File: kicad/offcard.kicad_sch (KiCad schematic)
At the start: 25 parts, among them IC1 NAU7802KGI, J10 lower fan, J4 heater, J5 5kg load cell, J6 LCD, J7 upper fan, Q2 SSM3K127TU, Q3 T1210-800G

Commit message: v1.7.0 upgrade most C/R to 1206 from 0805
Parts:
- R1, R12, R5: footprint PCM_Resistor_SMD_AKL:R_0805_2012Metric_Pad1.15x1.40mm_HandSolder -> Resistor_SMD:R_1206_3216Metric_Pad1.30x1.75mm_HandSolder
- R2, R3, R4: footprint Resistor_SMD:R_0805_2012Metric_Pad1.20x1.40mm_HandSolder -> Resistor_SMD:R_1206_3216Metric_Pad1.30x1.75mm_HandSolder
- R7: footprint PCM_Resistor_SMD_AKL:R_0805_2012Metric_Pad1.15x1.40mm_HandSolder -> PCM_Resistor_SMD_AKL:R_1206_3216Metric_Pad1.30x1.75mm_HandSolder
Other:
- note added: "2A/4A max continuous/pulse drain current. 10mA max current to MOSFET: 3.3V / 0.01A = 330Ω (0.033W). Schottky diode across motor +/- for EMP protection. Greartisan draws 0.18A at 12V (2.16W) in steady state. Can possibly eliminate R7 if MotorPin is always OUTPUT."
- note removed: "2A/4A max continuous/pulse drain current. 10mA max current to MOSFET: 3.3V / 0.01A = 330Ω (0.033W). Schottky diode across motor +/- for EMP protection. Greartisan draws 0.18A at 12V (2.16W) in steady state."
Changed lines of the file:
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@@
 	(title_block
 		(title "dankdryer")
-		(date "2025-02-16")
-		(rev "1.6.0")
+		(date "2025-02-18")
+		(rev "1.7.0")
 		(company "dirty south supercomputing")
 		(comment 1 "nick black")
@@
 		)
 	)
-	(text "2A/4A max continuous/pulse drain current.\n10mA max current to MOSFET: 3.3V / 0.01A = 330Ω (0.033W).\nSchottky diode across motor +/- for EMP protection.\nGreartisan draws 0.18A at 12V (2.16W) in steady state."
+	(text "2A/4A max continuous/pulse drain current.\n10mA max current to MOSFET: 3.3V / 0.01A = 330Ω (0.033W).\nSchottky diode across motor +/- for EMP protection.\nGreartisan draws 0.18A at 12V (2.16W) in steady state.\nCan possibly eliminate R7 if MotorPin is always OUTPUT."
 		(exclude_from_sim no)
-		(at 97.79 97.282 0)
+		(at 97.79 95.504 0)
 		(effects
 			(font
@@
 			)
 		)
-		(property "Footprint" "PCM_Resistor_SMD_AKL:R_0805_2012Metric_Pad1.15x1.40mm_HandSolder"
+		(property "Footprint" "Resistor_SMD:R_1206_3216Metric_Pad1.30x1.75mm_HandSolder"
 			(at 31.242 49.53 90)
 			(effects
@@
 			)
 		)
-		(property "Footprint" "PCM_Resistor_SMD_AKL:R_0805_2012Metric_Pad1.15x1.40mm_HandSolder"
+		(property "Footprint" "PCM_Resistor_SMD_AKL:R_1206_3216Metric_Pad1.30x1.75mm_HandSolder"
 			(at 118.872 62.23 90)
 			(effects
@@
 			)
 		)
-		(property "Footprint" "Resistor_SMD:R_0805_2012Metric_Pad1.20x1.40mm_HandSolder"
+		(property "Footprint" "Resistor_SMD:R_1206_3216Metric_Pad1.30x1.75mm_HandSolder"
 			(at 35.56 122.428 90)
 			(effects
@@
 			)
 		)
-		(property "Footprint" "Resistor_SMD:R_0805_2012Metric_Pad1.20x1.40mm_HandSolder"
+		(property "Footprint" "Resistor_SMD:R_1206_3216Metric_Pad1.30x1.75mm_HandSolder"
 			(at 50.292 139.7 90)
 			(effects
@@
 			)
 		)
-		(property "Footprint" "PCM_Resistor_SMD_AKL:R_0805_2012Metric_Pad1.15x1.40mm_HandSolder"
+		(property "Footprint" "Resistor_SMD:R_1206_3216Metric_Pad1.30x1.75mm_HandSolder"
 			(at 69.342 44.45 90)
 			(effects
@@
 			)
 		)
-		(property "Footprint" "Resistor_SMD:R_0805_2012Metric_Pad1.20x1.40mm_HandSolder"
+		(property "Footprint" "Resistor_SMD:R_1206_3216Metric_Pad1.30x1.75mm_HandSolder"
 			(at 52.07 122.428 90)
 			(effects
@@
 			)
 		)
-		(property "Footprint" "PCM_Resistor_SMD_AKL:R_0805_2012Metric_Pad1.15x1.40mm_HandSolder"
+		(property "Footprint" "Resistor_SMD:R_1206_3216Metric_Pad1.30x1.75mm_HandSolder"
 			(at 132.08 60.198 90)
 			(effects

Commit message: 1.7.2: move fan capacitors to 1206
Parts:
- C15, C16: footprint Capacitor_SMD:C_0805_2012Metric_Pad1.18x1.45mm_HandSolder -> Capacitor_SMD:C_1206_3216Metric_Pad1.33x1.80mm_HandSolder
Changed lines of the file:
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@@
 		(title "dankdryer")
 		(date "2025-02-18")
-		(rev "1.7.0")
+		(rev "1.7.2")
 		(company "dirty south supercomputing")
 		(comment 1 "nick black")
@@
 			)
 		)
-		(property "Footprint" "Capacitor_SMD:C_0805_2012Metric_Pad1.18x1.45mm_HandSolder"
+		(property "Footprint" "Capacitor_SMD:C_1206_3216Metric_Pad1.33x1.80mm_HandSolder"
 			(at 72.0852 73.66 0)
 			(effects
@@
 			)
 		)
-		(property "Footprint" "Capacitor_SMD:C_0805_2012Metric_Pad1.18x1.45mm_HandSolder"
+		(property "Footprint" "Capacitor_SMD:C_1206_3216Metric_Pad1.33x1.80mm_HandSolder"
 			(at 33.9852 77.47 0)
 			(effects

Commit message: invert logic for gpio9, erp
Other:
- moved on the sheet: C16, J7, R1, R9
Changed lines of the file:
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@@
 	(title_block
 		(title "dankdryer")
-		(date "2025-02-18")
-		(rev "1.7.2")
+		(date "2025-02-21")
+		(rev "1.7.3")
 		(company "dirty south supercomputing")
 		(comment 1 "nick black")
@@
 	)
 	(junction
-		(at 33.02 62.23)
+		(at 33.02 58.42)
 		(diameter 0)
 		(color 0 0 0 0)
@@
 	)
 	(junction
-		(at 33.02 69.85)
+		(at 33.02 66.04)
 		(diameter 0)
 		(color 0 0 0 0)
@@
 	(wire
 		(pts
-			(xy 33.02 53.34) (xy 33.02 62.23)
+			(xy 33.02 49.53) (xy 33.02 58.42)
 		)
 		(stroke
@@
 	(wire
 		(pts
-			(xy 33.02 69.85) (xy 40.64 69.85)
+			(xy 33.02 66.04) (xy 40.64 66.04)
 		)
 		(stroke
@@
 	(wire
 		(pts
-			(xy 30.48 36.83) (xy 30.48 62.23)
+			(xy 30.48 33.02) (xy 30.48 58.42)
 		)
 		(stroke
@@
 	(wire
 		(pts
-			(xy 35.56 62.23) (xy 40.64 62.23)
+			(xy 35.56 58.42) (xy 40.64 58.42)
 		)
 		(stroke
@@
 				(size 2.54 2.54)
 			)
-			(justify right top)
+			(justify left top)
 		)
 	)
@@
 	(global_label "UPWM"
 		(shape input)
-		(at 40.64 62.23 0)
+		(at 40.64 58.42 0)
 		(fields_autoplaced yes)
 		(effects
@@
 		)
 		(property "Intersheetrefs" "${INTERSHEET_REFS}"
-			(at 49.1285 62.23 0)
+			(at 49.1285 58.42 0)
 			(effects
 				(font
@@
 	(global_label "UTach"
 		(shape input)
-		(at 40.64 69.85 0)
+		(at 40.64 66.04 0)
 		(fields_autoplaced yes)
 		(effects
@@
 		)
 		(property "Intersheetrefs" "${INTERSHEET_REFS}"
-			(at 49.3099 69.85 0)
+			(at 49.3099 66.04 0)
 			(effects
 				(font
@@
 	(symbol
 		(lib_id "Connector_Generic:Conn_01x04")
-		(at 30.48 57.15 90)
+		(at 30.48 53.34 90)
 		(unit 1)
 		(exclude_from_sim no)
@@
 		(dnp no)
 		(property "Reference" "J7"
-			(at 41.91 58.928 90)
+			(at 41.91 55.118 90)
 			(effects
 				(font
@@
 		)
 		(property "Value" "upper fan"
-			(at 42.418 56.642 90)
+			(at 42.418 52.832 90)
 			(effects
 				(font
@@
 		)
 		(property "Footprint" "Connector:FanPinHeader_1x04_P2.54mm_Vertical"
-			(at 30.48 57.15 0)
+			(at 30.48 53.34 0)
 			(effects
 				(font
@@
 		)
 		(property "Datasheet" "~"
-			(at 30.48 57.15 0)
+			(at 30.48 53.34 0)
 			(effects
 				(font
@@
 		)
 		(property "Description" "Generic connector, single row, 01x04, script generated (kicad-library-utils/schlib/autogen/connector/)"
-			(at 30.48 57.15 0)
+			(at 30.48 53.34 0)
 			(effects
 				(font
@@
 	(symbol
 		(lib_id "Device:R")
-		(at 33.02 49.53 0)
+		(at 33.02 45.72 0)
 		(unit 1)
 		(exclude_from_sim no)
@@
 		(dnp no)
 		(property "Reference" "R1"
-			(at 35.814 48.26 0)
+			(at 35.814 44.45 0)
 			(effects
 				(font
@@
 		)
 		(property "Value" "680"
-			(at 35.814 51.054 0)
+			(at 35.814 47.244 0)
 			(effects
 				(font
@@
 		)
 		(property "Footprint" "Resistor_SMD:R_1206_3216Metric_Pad1.30x1.75mm_HandSolder"
-			(at 31.242 49.53 90)
+			(at 31.242 45.72 90)
 			(effects
 				(font
@@
 		)
 		(property "Datasheet" "~"
-			(at 33.02 49.53 0)
+			(at 33.02 45.72 0)
 			(effects
 				(font
@@
 		)
 		(property "Description" "Resistor"
-			(at 33.02 49.53 0)
+			(at 33.02 45.72 0)
 			(effects
 				(font
@@
 	(symbol
 		(lib_id "power:GND")
-		(at 27.94 62.23 0)
+		(at 27.94 58.42 0)
 		(unit 1)
 		(exclude_from_sim no)
@@
 		(dnp no)
 		(property "Reference" "#PWR035"
-			(at 27.94 68.58 0)
+			(at 27.94 64.77 0)
 			(effects
 				(font
@@
 		)
 		(property "Value" "GND"
-			(at 28.194 66.802 0)
+			(at 28.194 62.992 0)
 			(effects
 				(font
@@
 		)
 		(property "Footprint" ""
-			(at 27.94 62.23 0)
+			(at 27.94 58.42 0)
 			(effects
 				(font
@@
 		)
 		(property "Datasheet" ""
-			(at 27.94 62.23 0)
+			(at 27.94 58.42 0)
 			(effects
 				(font
@@
 		)
 		(property "Description" "Power symbol creates a global label with name \"GND\" , ground"
-			(at 27.94 62.23 0)
+			(at 27.94 58.42 0)
 			(effects
 				(font
@@
 	(symbol
 		(lib_id "power:GND")
-		(at 33.02 77.47 0)
+		(at 33.02 73.66 0)
 		(unit 1)
 		(exclude_from_sim no)
@@
 		(dnp no)
 		(property "Reference" "#PWR025"
-			(at 33.02 83.82 0)
+			(at 33.02 80.01 0)
 			(effects
 				(font
@@
 		)
 		(property "Value" "GND"
-			(at 33.274 82.042 0)
+			(at 33.274 78.232 0)
 			(effects
 				(font
@@
 		)
 		(property "Footprint" ""
-			(at 33.02 77.47 0)
+			(at 33.02 73.66 0)
 			(effects
 				(font
@@
 		)
 		(property "Datasheet" ""
-			(at 33.02 77.47 0)
+			(at 33.02 73.66 0)
 			(effects
 				(font
@@
 		)
 		(property "Description" "Power symbol creates a global label with name \"GND\" , ground"
-			(at 33.02 77.47 0)
+			(at 33.02 73.66 0)
 			(effects
 				(font
@@
 	(symbol
 		(lib_id "power:+12V")
-		(at 30.48 36.83 0)
+		(at 30.48 33.02 0)
 		(unit 1)
 		(exclude_from_sim no)
@@
 		(dnp no)
 		(property "Reference" "#PWR08"
-			(at 30.48 40.64 0)
+			(at 30.48 36.83 0)
 			(effects
 				(font
@@
 		)
 		(property "Value" "+12V"
-			(at 30.48 31.75 0)
+			(at 30.48 27.94 0)
 			(effects
 				(font
@@
 		)
 		(property "Footprint" ""
-			(at 30.48 36.83 0)
+			(at 30.48 33.02 0)
 			(effects
 				(font
@@
 		)
 		(property "Datasheet" ""
-			(at 30.48 36.83 0)
+			(at 30.48 33.02 0)
 			(effects
 				(font
@@
 		)
 		(property "Description" "Power symbol creates a global label with name \"+12V\""
-			(at 30.48 36.83 0)
+			(at 30.48 33.02 0)
 			(effects
 				(font
@@
 	(symbol
 		(lib_id "power:+3.3V")
-		(at 33.02 45.72 0)
+		(at 33.02 41.91 0)
 		(unit 1)
 		(exclude_from_sim no)
@@
 		(dnp no)
 		(property "Reference" "#PWR06"
-			(at 33.02 49.53 0)
+			(at 33.02 45.72 0)
 			(effects
 				(font
@@
 		)
 		(property "Value" "+3.3V"
-			(at 29.972 41.656 0)
+			(at 29.972 37.846 0)
 			(effects
 				(font
@@
 		)
 		(property "Footprint" ""
-			(at 33.02 45.72 0)
+			(at 33.02 41.91 0)
 			(effects
 				(font
@@
 		)
 		(property "Datasheet" ""
-			(at 33.02 45.72 0)
+			(at 33.02 41.91 0)
 			(effects
 				(font
@@
 		)
 		(property "Description" "Power symbol creates a global label with name \"+3.3V\""
-			(at 33.02 45.72 0)
+			(at 33.02 41.91 0)
 			(effects
 				(font
@@
 	(symbol
 		(lib_id "Device:R")
-		(at 33.02 66.04 0)
+		(at 33.02 62.23 0)
 		(unit 1)
 		(exclude_from_sim no)
@@
 		(fields_autoplaced yes)
 		(property "Reference" "R9"
-			(at 35.56 64.7699 0)
+			(at 35.56 60.9599 0)
 			(effects
 				(font
@@
 		)
 		(property "Value" "15k"
-			(at 35.56 67.3099 0)
+			(at 35.56 63.4999 0)
 			(effects
 				(font
@@
 		)
 		(property "Footprint" "PCM_Resistor_SMD_AKL:R_1206_3216Metric_Pad1.30x1.75mm"
-			(at 31.242 66.04 90)
+			(at 31.242 62.23 90)
 			(effects
 				(font
@@
 		)
 		(property "Datasheet" "~"
-			(at 33.02 66.04 0)
+			(at 33.02 62.23 0)
 			(effects
 				(font
@@
 		)
 		(property "Description" "Resistor"
-			(at 33.02 66.04 0)
+			(at 33.02 62.23 0)
 			(effects
 				(font
@@
 	(symbol
 		(lib_id "Device:C")
-		(at 33.02 73.66 0)
+		(at 33.02 69.85 0)
 		(unit 1)
 		(exclude_from_sim no)
@@
 		(fields_autoplaced yes)
 		(property "Reference" "C16"
-			(at 36.83 72.3899 0)
+			(at 36.83 68.5799 0)
 			(effects
 				(font
@@
 		)
 		(property "Value" "1n"
-			(at 36.83 74.9299 0)
+			(at 36.83 71.1199 0)
 			(effects
 				(font
@@
 		)
 		(property "Footprint" "Capacitor_SMD:C_1206_3216Metric_Pad1.33x1.80mm_HandSolder"
-			(at 33.9852 77.47 0)
+			(at 33.9852 73.66 0)
 			(effects
 				(font
@@
 		)
 		(property "Datasheet" "~"
-			(at 33.02 73.66 0)
+			(at 33.02 69.85 0)
 			(effects
 				(font
@@
 		)
 		(property "Description" "Unpolarized capacitor"
-			(at 33.02 73.66 0)
+			(at 33.02 69.85 0)
 			(effects
 				(font

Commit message: switch from AKL_R to regular
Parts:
- R7: footprint PCM_Resistor_SMD_AKL:R_1206_3216Metric_Pad1.30x1.75mm_HandSolder -> Resistor_SMD:R_1206_3216Metric_Pad1.30x1.75mm_HandSolder
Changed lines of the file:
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@@
 			)
 		)
-		(property "Footprint" "PCM_Resistor_SMD_AKL:R_1206_3216Metric_Pad1.30x1.75mm_HandSolder"
+		(property "Footprint" "Resistor_SMD:R_1206_3216Metric_Pad1.30x1.75mm_HandSolder"
 			(at 118.872 62.23 90)
 			(effects

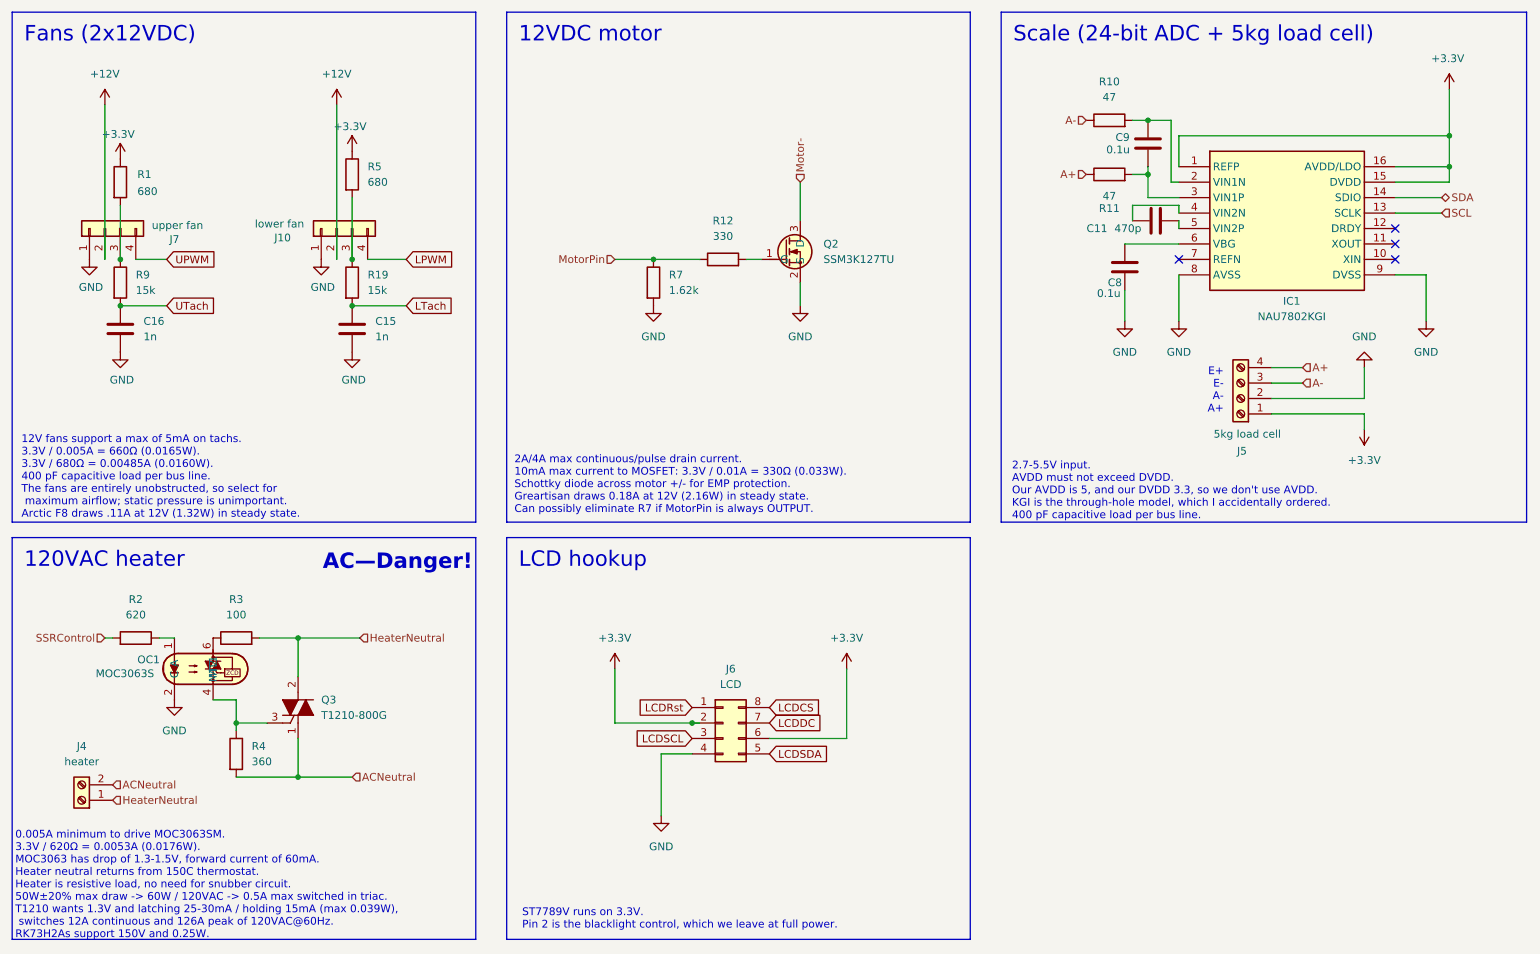
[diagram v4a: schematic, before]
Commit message: upgrade to kicad9
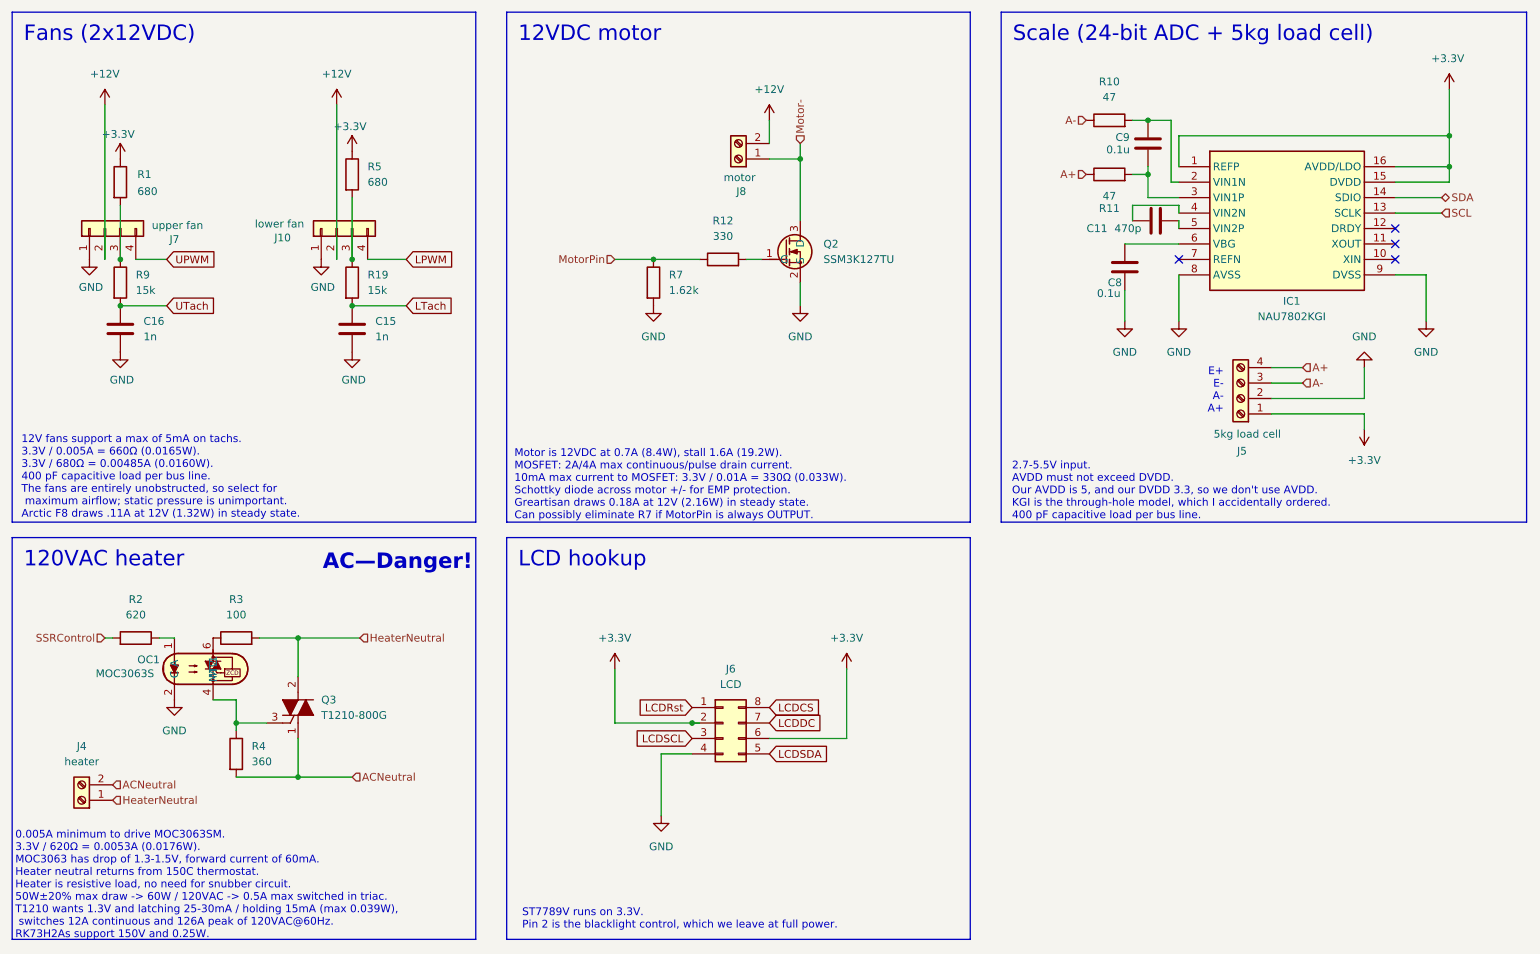
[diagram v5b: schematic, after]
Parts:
- added J8: motor, TerminalBlock:TerminalBlock_bornier-2_P5.08mm, symbol Connector:Screw_Terminal_01x02
- J4: footprint dank:TerminalBlock_bornier-2_P5.08mm -> TerminalBlock:TerminalBlock_bornier-2_P5.08mm
- J5: footprint dank:TerminalBlock_bornier-4_P5.08mm -> TerminalBlock:TerminalBlock_bornier-4_P5.08mm
- Q2: footprint PCM_Package_TO_SOT_SMD_AKL:SOT-323_SC-70 -> dank:UFM_TOS
- Q3: footprint PCM_Package_TO_SOT_SMD_AKL:TO-263-2 -> dank:T1210-800G-TR
- R10, R11: footprint PCM_Resistor_SMD_AKL:R_0805_2012Metric_Pad1.15x1.40mm_HandSolder -> Resistor_SMD:R_1206_3216Metric_Pad1.30x1.75mm_HandSolder
- R19, R9: footprint PCM_Resistor_SMD_AKL:R_1206_3216Metric_Pad1.30x1.75mm -> Resistor_SMD:R_1206_3216Metric_Pad1.30x1.75mm_HandSolder
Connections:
- net +12V: now also J8.2 (Pin_2)
- net Motor-: now also J8.1 (Pin_1)
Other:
- note added: "Motor is 12VDC at 0.7A (8.4W), stall 1.6A (19.2W). MOSFET: 2A/4A max continuous/pulse drain current. 10mA max current to MOSFET: 3.3V / 0.01A = 330Ω (0.033W). Schottky diode across motor +/- for EMP protection. Greartisan draws 0.18A at 12V (2.16W) in steady state. Can possibly eliminate R7 if MotorPin is always OUTPUT."
- note removed: "2A/4A max continuous/pulse drain current. 10mA max current to MOSFET: 3.3V / 0.01A = 330Ω (0.033W). Schottky diode across motor +/- for EMP protection. Greartisan draws 0.18A at 12V (2.16W) in steady state. Can possibly eliminate R7 if MotorPin is always OUTPUT."
